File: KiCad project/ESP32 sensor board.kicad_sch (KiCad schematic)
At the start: 33 parts, among them J1 USB_C_Receptacle, J3 JST_2mm_LiPo, U1 MCP73871, U2 AMS1117-3.3

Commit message: Fixed lots of bugs.
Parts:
- removed C3: 100u, Capacitor_SMD:C_0805_2012Metric, symbol SparkFun-Capacitor:C
- removed C4: 10u, Capacitor_SMD:C_0805_2012Metric, symbol SparkFun-Capacitor:C
- removed C6: 4.7u, Capacitor_SMD:C_0805_2012Metric, symbol SparkFun-Capacitor:C
- removed C9: 100u, Capacitor_SMD:C_0805_2012Metric, symbol SparkFun-Capacitor:C_Polarized
- removed D1: PESD5V0S1UL_315, Footprints:DIO_PESD5V0S1UL_315, symbol PESD5V0S1UL_315:PESD5V0S1UL_315
- removed D2: SS14, SparkFun-Semiconductor-Standard:SMA, symbol SparkFun-DiscreteSemi:D_Schottky_1A_40V_0.5V
- removed R10, R2, R9: 10K, Resistor_SMD:R_0805_2012Metric, symbol Device:R
- added C2: 0.1u, Capacitor_SMD:C_0805_2012Metric, symbol SparkFun-Capacitor:C
- C5: value 4.7u -> 0.1u; Purpose Decoupling capacitor. -> Bypass capacitor.
- D1: renamed from D3; footprint SparkFun-LED:LED_0603_1608Metric -> LED_SMD:LED_0603_1608Metric
- D4: renamed from D11; footprint SparkFun-LED:LED_0603_1608Metric -> LED_SMD:LED_0603_1608Metric
- R4: renamed from R12; now not fitted
- renumbered C23 to C1, C1 to C3, C2 to C4, C7 to C6, D4 to D2, D5 to D3, J3 to J2, R7 to R1, R26 to R10, R8 to R2, R11 to R3, R1 to R5, R3 to R6, R4 to R7, R5 to R8, R6 to R9
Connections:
- net +5V_USB: now also U1.17 (CE), U1.4 (PROG2); no longer C3.1, C5.2, U1.1 (OUT), U1.20 (OUT), U2.3 (VI)
- net 3.3V: now also C5.1
- net GND: now also C1.2, C5.2, U1.3 (SEL), C2.2; no longer C1.1, C5.1
- net at J1.VBUS: now also C1.1, F1.1; no longer C1.2
- new net +5V: C2.1, C3.1, U1.1 (OUT), U1.20 (OUT), U2.3 (VI)
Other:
- sheet ESP32-C3-02 ports: added VBUS; removed none
- moved on the sheet: C1, C3, C4, F1, U2

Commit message: Configured the layout editor.
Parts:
- D2, D3: footprint SparkFun-LED:LED_0603_1608Metric -> LED_SMD:LED_0603_1608Metric
- F1: footprint SparkFun-Fuse:1210 -> Project_Library:1210
- J1: footprint SparkFun-Connector:USB-C_16 -> Project_Library:USB-C_16
- J2: footprint SparkFun-Connector:JST_SMD_2.0mm-2 -> Project_Library:JST_SMD_2.0mm-2
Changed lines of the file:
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@@
 			)
 		)
-		(property "Footprint" "SparkFun-Connector:USB-C_16"
+		(property "Footprint" "Project_Library:USB-C_16"
 			(at 30.48 96.52 0)
 			(effects
@@
 			)
 		)
-		(property "Footprint" "SparkFun-LED:LED_0603_1608Metric"
+		(property "Footprint" "LED_SMD:LED_0603_1608Metric"
 			(at 160.02 114.3 0)
 			(effects
@@
 			)
 		)
-		(property "Footprint" "SparkFun-Fuse:1210"
+		(property "Footprint" "Project_Library:1210"
 			(at 73.66 54.61 0)
 			(effects
@@
 			)
 		)
-		(property "Footprint" "SparkFun-LED:LED_0603_1608Metric"
+		(property "Footprint" "LED_SMD:LED_0603_1608Metric"
 			(at 170.18 115.57 0)
 			(effects
@@
 			)
 		)
-		(property "Footprint" "SparkFun-Connector:JST_SMD_2.0mm-2"
+		(property "Footprint" "Project_Library:JST_SMD_2.0mm-2"
 			(at 39.37 134.62 0)
 			(effects
@@
 		)
 		(instances
-			(project "KLP-5e-ESP32-sensor-board-main_modifications"
+			(project "ESP32 sensor board"
 				(path "/16c571a0-8550-4f05-972c-22b0701cbf02"
 					(page "2")

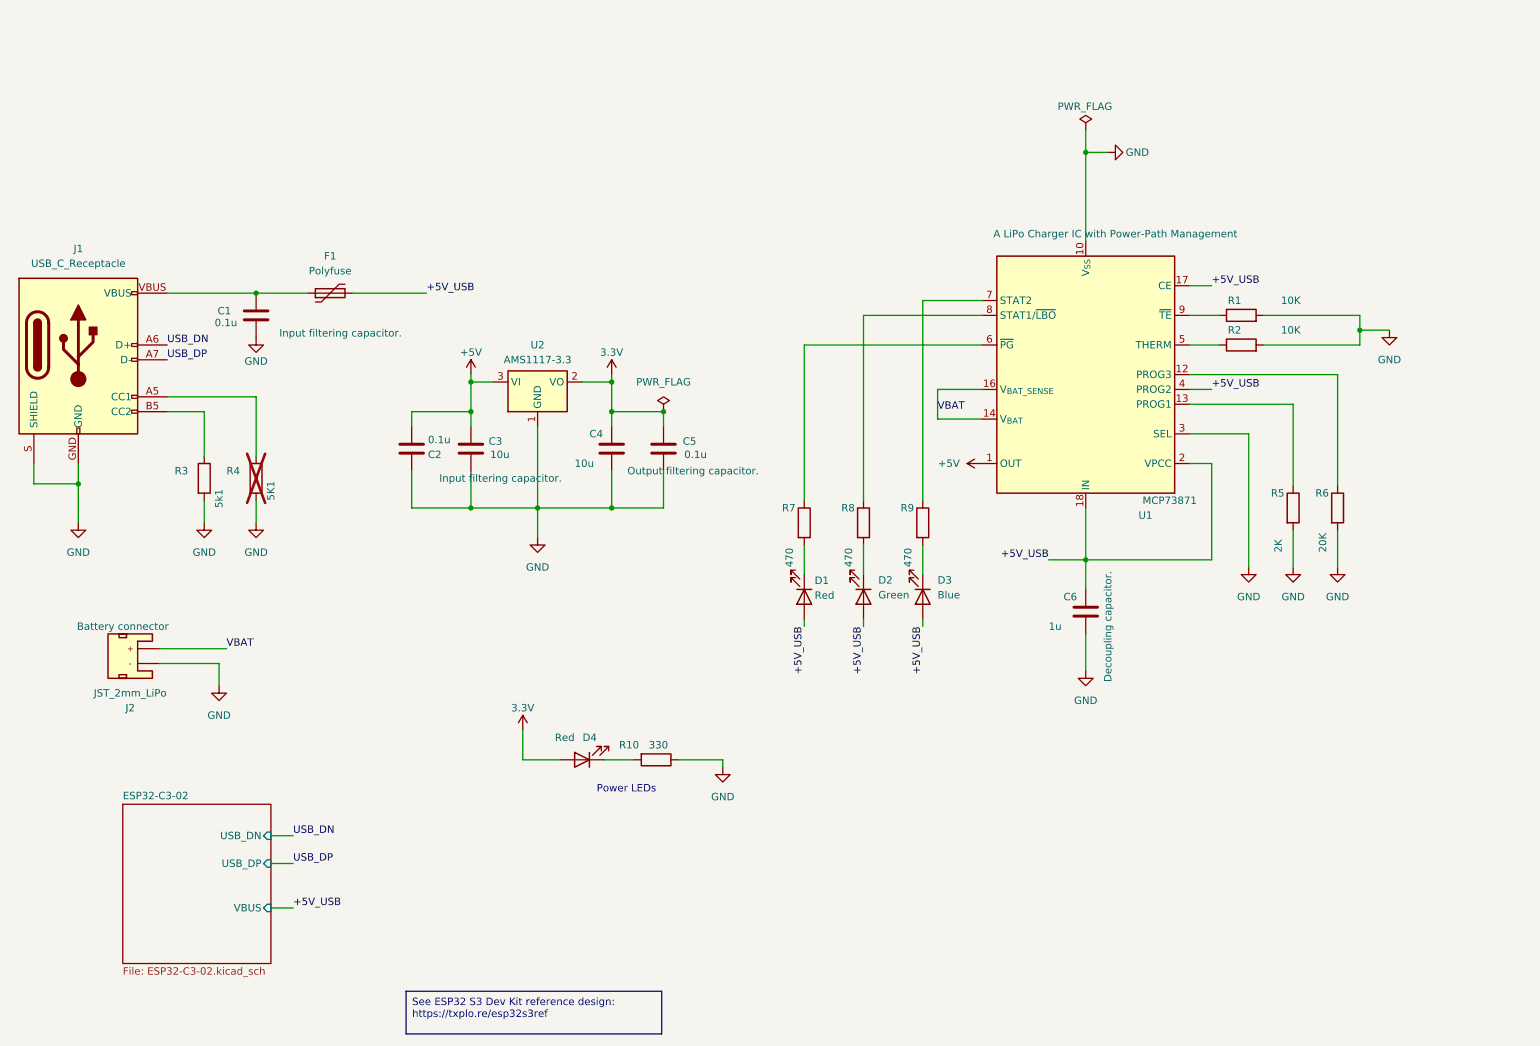
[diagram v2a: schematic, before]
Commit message: Trying routing, layout, and changed USB and battery connectors.
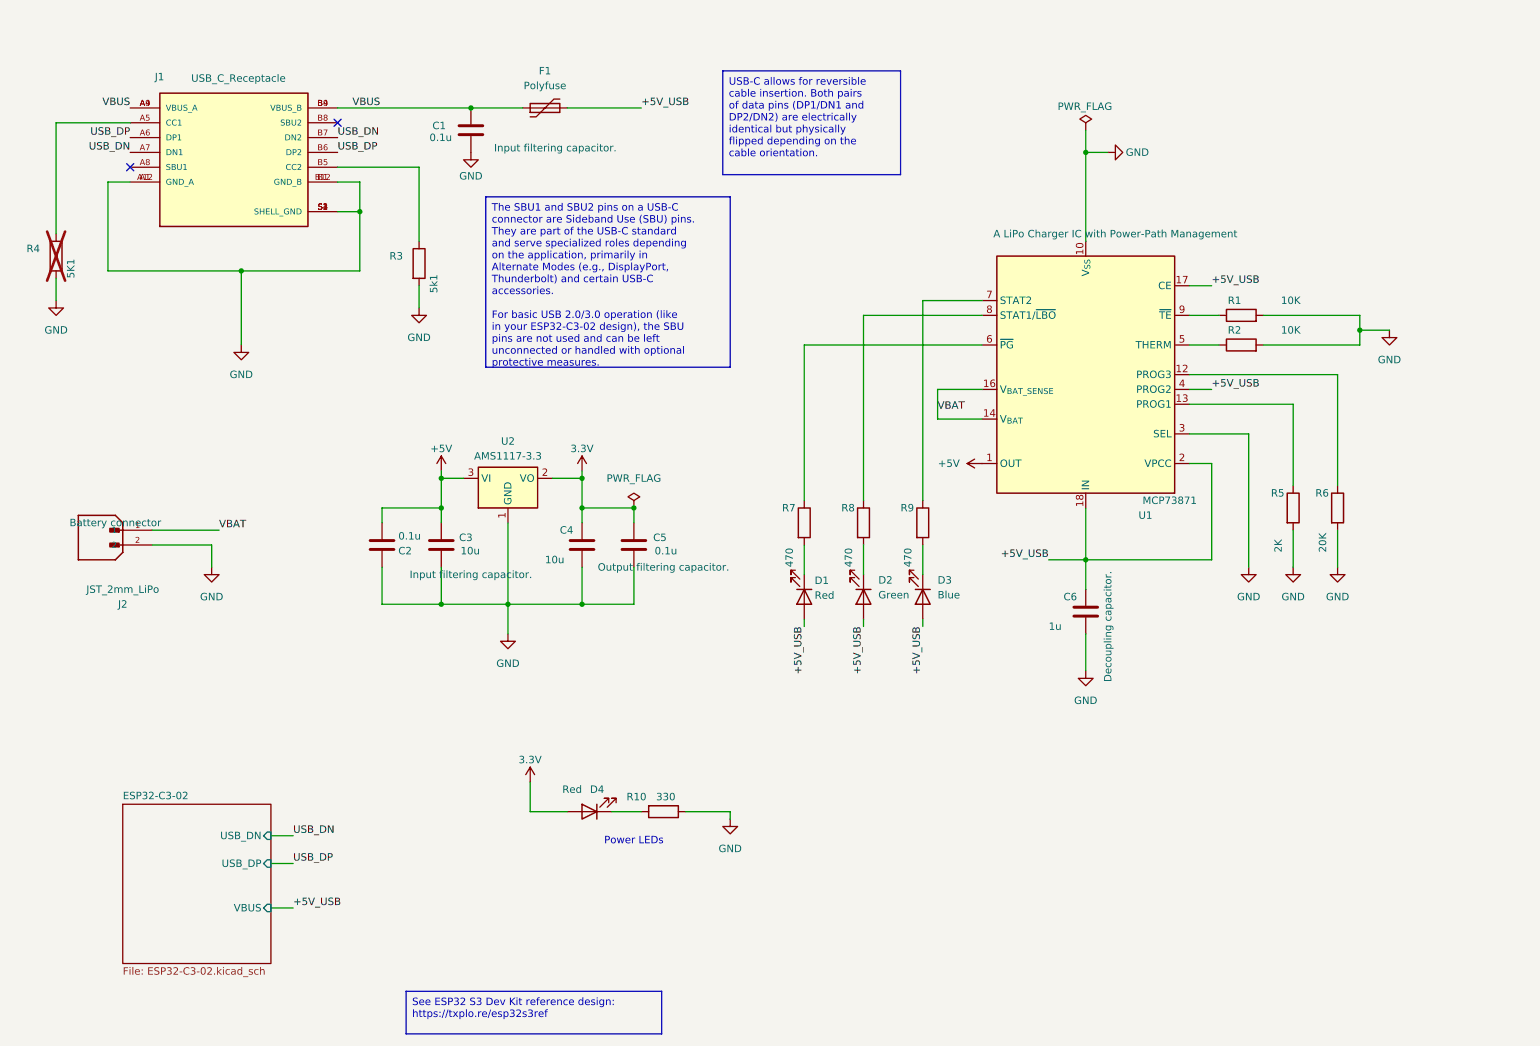
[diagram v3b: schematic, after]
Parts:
- J1: footprint Project_Library:USB-C_16 -> Footprints:VALCON_CSP-USC16-TR; symbol SparkFun-Connector:USB_C_Receptacle -> CSP-USC16-TR:CSP-USC16-TR; Availability (none) -> In Stock; Check_prices (none) -> https://www.snapeda.com/parts/CSP-USC16-TR/Valcon/view-part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; Description_1 (none) -> CSP-USC16-TR Valcon USB Type C Surface Mount PCB Socket; MANUFACTURER (none) -> Valcon; MAXIMUM_PACKAGE_HEIGHT (none) -> 3.26 mm; MF (none) -> Valcon; MP (none) -> CSP-USC16-TR; PARTREV (none) -> A0; Package (none) -> None; Price (none) -> None; STANDARD (none) -> Manufacturer Recommendations; SnapEDA_Link (none) -> https://www.snapeda.com/parts/CSP-USC16-TR/Valcon/view-part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
- J2: footprint Project_Library:JST_SMD_2.0mm-2 -> Footprints:JST_B2B-PH-SM4-TB; symbol SparkFun-Connector:Conn_01x02_JST_2mm_LiPo -> B2B-PH-SM4-TB:B2B-PH-SM4-TB; Availability (none) -> In Stock; Check_prices (none) -> https://www.snapeda.com/parts/B2B-PH-SM4-TB/JST/view-part/?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; Description_1 (none) -> Connector Header Surface Mount 2 position 0.079 (2.00mm); MANUFACTURER (none) -> JST; MAXIMUM_PACKAGE_HEIGHT (none) -> 6.6 mm; MF (none) -> JST; MP (none) -> B2B-PH-SM4-TB; PARTREV (none) -> N/A; Package (none) -> NON STANDARD-2 JST; Price (none) -> None; STANDARD (none) -> Manufacturer Recommendations; SnapEDA_Link (none) -> https://www.snapeda.com/parts/B2B-PH-SM4-TB/JST/view-part/?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
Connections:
- net GND: now also J1.A1 (GND_A), J1.A12 (GND_A), J1.B1 (GND_B), J1.B12 (GND_B), J1.S1 (SHELL_GND), J1.S2 (SHELL_GND), J1.S3 (SHELL_GND), J1.S4 (SHELL_GND), J2.2; no longer J1.GND, J1.S (SHIELD), J2.1 (-)
- net USB_DN: now also J1.A7 (DN1), J1.B7 (DN2); no longer J1.A6 (D+), J1.B6 (D+)
- net USB_DP: now also J1.A6 (DP1), J1.B6 (DP2); no longer J1.A7 (D-), J1.B7 (D-)
- net VBAT: now also J2.1; no longer J2.2 (+)
- net VBUS: now reaches C1.1, F1.1
- net VBUS: now also J1.A4 (VBUS_A), J1.A9 (VBUS_A), J1.B4 (VBUS_B), J1.B9 (VBUS_B); no longer J1.VBUS
- no-connect marks 0 -> 2
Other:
- moved on the sheet: C1, C2, C3, C4, C5, D4, F1, R10, R3, R4, U2

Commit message: Replaced the button, USB, bat connector with new symbols and footprints. Completed draft layout and routing.
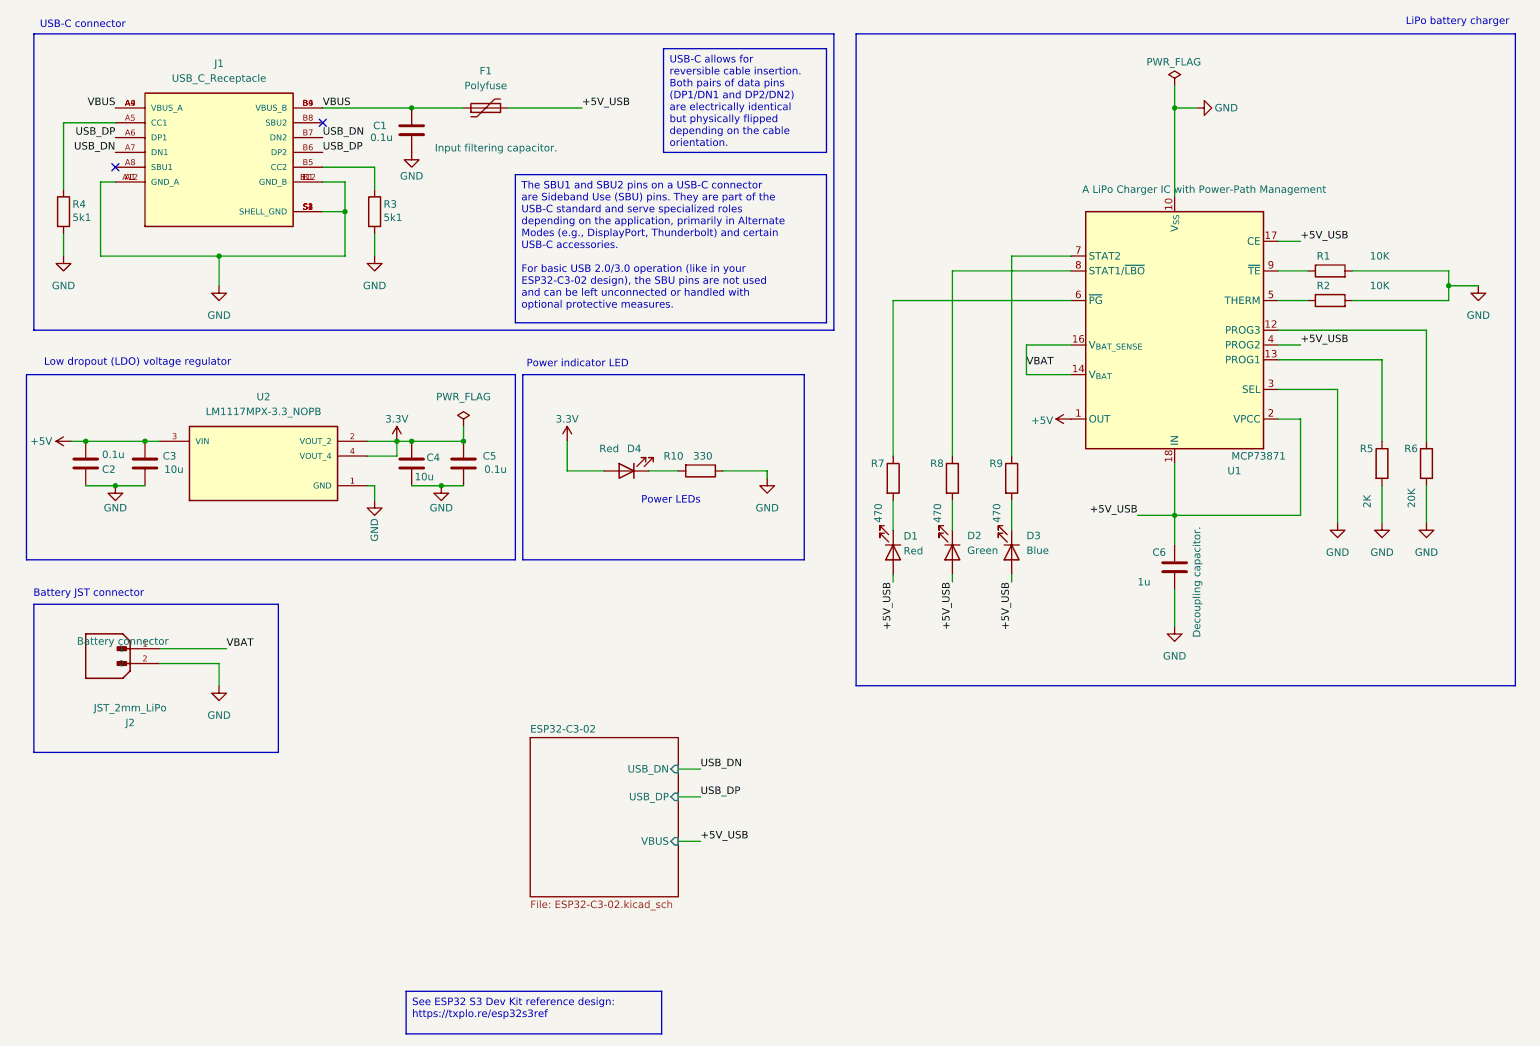
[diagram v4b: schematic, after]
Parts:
- removed U2: AMS1117-3.3, Package_TO_SOT_SMD:SOT-223-3_TabPin2, symbol Regulator_Linear:AMS1117-3.3
- added U2: LM1117MPX-3.3_NOPB, Footprints:VREG_LM1117MPX-3.3_NOPB, symbol LM1117MPX-3.3_NOPB:LM1117MPX-3.3_NOPB
- F1: footprint Project_Library:1210 -> Fuse:Fuse_1210_3225Metric
- J2: Manufacturer_Part_Number (none) -> ?
- R1, R10, R2, R3, R5, R6, R7, R8, R9: PACKAGE (none) -> 0805
- R4: value 5K1 -> 5k1; PACKAGE (none) -> 0805; now fitted
- U1: MANUFACTURER (none) -> Microchip; Manufacturer_Part_Number (none) -> MCP73871-4CCI/ML; PACKAGE (none) -> QFN-20
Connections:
- net +5V: now also U2.3 (VIN)
- net 3.3V: now also U2.2 (VOUT_2), U2.4 (VOUT_4)
- net GND: now also U2.1 (GND)
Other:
- note added: "Battery JST connector"
- note added: "LiPo battery charger"
- note added: "Low dropout (LDO) voltage regulator"
- note added: "Power indicator LED"
- note added: "USB-C connector"
- moved on the sheet: C1, C2, C3, C4, C5, C6, D1, D2, D3, D4, F1, J1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
